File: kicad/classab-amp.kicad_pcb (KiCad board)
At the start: 2 copper layers, 62.6 x 114.6 mm, 75 parts, among them J3 INPUT, Q1 2N5401, Q10 IRFP9240, Q11 2N5551, Q12 2N5551, Q13 BD139, Q14 BD140, Q15 2N5551, Q16 BD140, Q2 2N5401, Q3 2N5401, Q4 2N5401, Q5 2N5551, Q6 2N5401, Q7 BD139, Q8 BD139, Q9 IRFP240

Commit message: Release candidate 1
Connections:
- net /LTP COM renamed Net-(Q2-E)

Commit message: Power supply work
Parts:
- R3, R5: value 470 -> 100
- R4: value 1k -> 470
- moved R5 9.59 mm to (231.4, 144.5)
- moved C11 3.22 mm to (239.8, 54.4)
- moved R3 1.78 mm to (231.4, 149.6)
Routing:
- net B+: track 146.5 -> 141.6 mm
- net Net-(Q5-E): track 11.6 -> 7.39 mm
- net Net-(C11-Pad2): track 12.1 -> 8.52 mm
- net Net-(Q11-E): track 11.4 -> 13.2 mm
- net PWRGND: track 351.6 -> 351.1 mm
- net B-: track 126.5 -> 126.0 mm

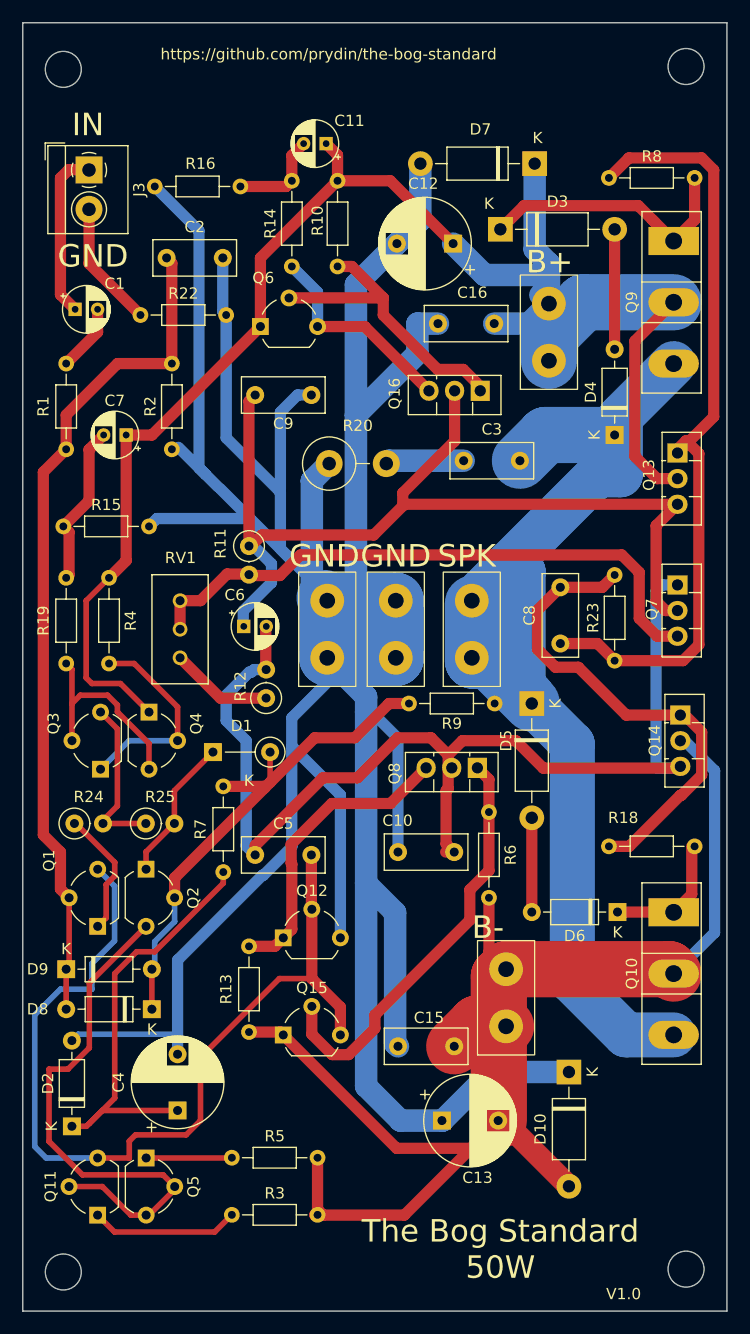
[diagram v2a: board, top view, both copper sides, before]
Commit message: Adjusted some component positioning
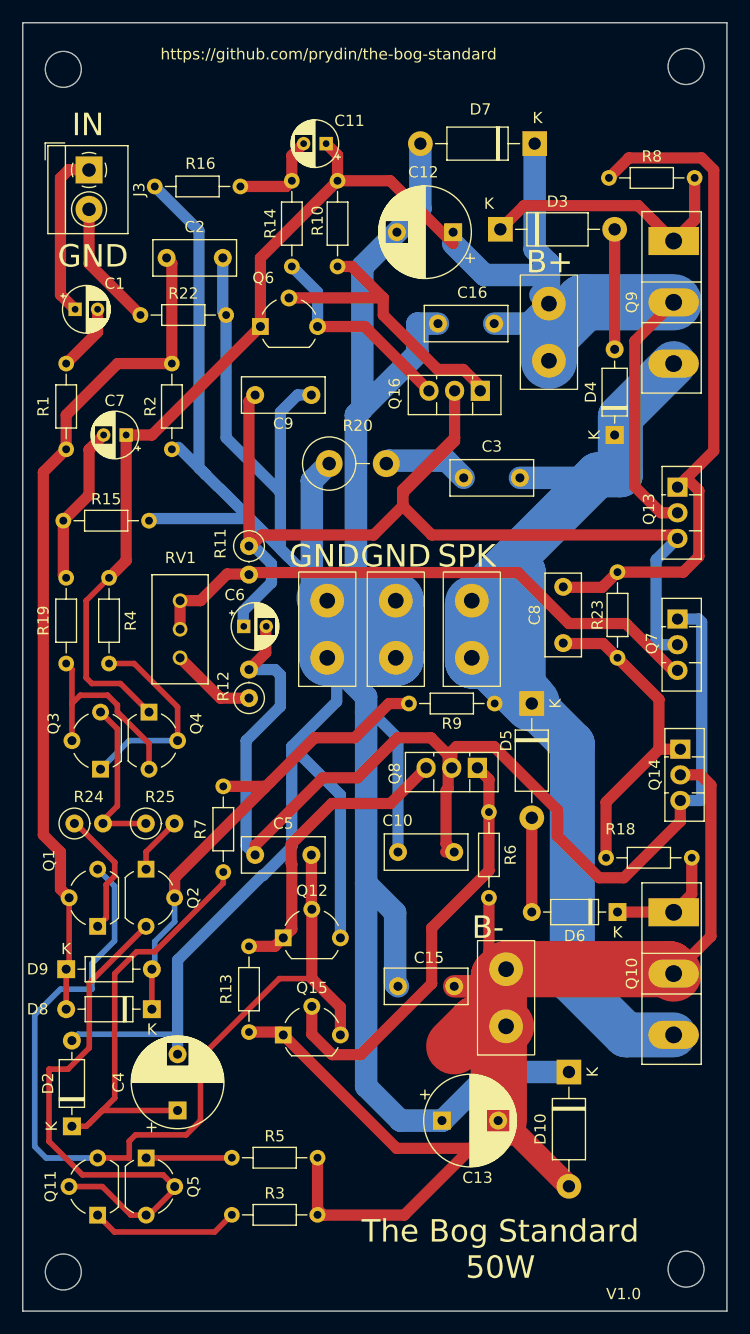
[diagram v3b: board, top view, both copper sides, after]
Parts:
- removed D1: 1N4148, Diode_THT:D_DO-35_SOD27_P5.08mm_Vertical_KathodeUp
- moved R23 7.88 mm to (265.7, 92.5), turned to -90 degrees
- moved C15 5.33 mm to (251.2, 129.3)
- moved C8 5.05 mm to (260.9, 93.8), turned to -90 degrees
- moved Q13 3.04 mm to (271.0, 84.9)
- moved Q7 3.04 mm to (271.0, 96.6)
- moved Q14 3.04 mm to (271.3, 108.2)
- moved D7 1.78 mm to (258.3, 54.4)
- moved C3 1.52 mm to (257.0, 84.1)
- moved R12 1.52 mm to (232.9, 103.7)
- moved R18 1.05 mm to (264.7, 117.9)
- moved C12 1.02 mm to (251.1, 62.2)
- moved R15 0.51 mm to (216.4, 87.9)
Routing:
- net Net-(Q14-E): track 43.6 -> 28.4 mm
- net Net-(Q14-B): track 97.6 -> 109.7 mm
- net Net-(Q13-E): track 70.2 -> 60.5 mm
- net Net-(Q13-B): track 86.2 -> 95.5 mm
- net Net-(Q2-E): track 12.9 -> 5.11 mm
- net B+: track 141.6 -> 146.2 mm
- net PWRGND: track 351.1 -> 347.3 mm
- net Net-(D8-K): track 45.8 -> 43.2 mm
- net Net-(Q7-B): track 54.0 -> 51.7 mm
- net /SPEAKER: track 105.8 -> 103.4 mm
- net B-: track 126.0 -> 128.2 mm
- net Net-(R12-Pad1): track 9.14 -> 7.61 mm
- net Net-(D6-K): track 11.5 -> 10.5 mm
- net Net-(C3-Pad2): track 6.99 -> 7.62 mm
- net Net-(Q15-B): track 37.6 -> 38.2 mm

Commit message: V1.1
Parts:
- removed the R22 at (223.3, 69.6)
- added J2: VOLUME, TerminalBlock_4Ucon:TerminalBlock_4Ucon_1x03_P3.50mm_Horizontal, F.Cu at (217.4, 70.5)
- added R2: 100, Resistor_THT:R_Axial_DIN0204_L3.6mm_D1.6mm_P7.62mm_Horizontal, F.Cu at (224.3, 68.3)
- added R3: 470, Resistor_THT:R_Axial_DIN0204_L3.6mm_D1.6mm_P7.62mm_Horizontal, F.Cu at (224.3, 72.1)
- C1: renamed from C2; value 100p -> 220p
- C6: renamed from C5; value 33p -> 47p
- C8: renamed from C9; value 68p -> 47p
- C9: renamed from C10; value 68p -> 47p
- R1: value 150 -> 1k
- R19: renamed from R10; value 47 -> 56
- R20: renamed from R6; value 22 -> 33
- moved C3 7.46 mm to (219.7, 76.2)
- moved R4 5.33 mm to (226.1, 76.2), turned to -90 degrees
- moved R1 3.06 mm to (216.4, 77.0)
- moved R16 2.29 mm to (232.2, 55.9)
- moved C2 1.78 mm to (222.0, 82.0)
- moved J1 1.76 mm to (217.4, 57.9), turned to 90 degrees
- moved C1 0.76 mm to (225.6, 63.8)
- moved R23 0.25 mm to (264.9, 117.9)
- renumbered C8 to C10, C16 to C11, C15 to C12, C12 to C13, C13 to C14, C3 to C15, C7 to C2, C1 to C3, C11 to C5, C6 to C7, D8 to D1, D9 to D2, D2 to D3, D3 to D4, D4 to D5, D5 to D6, D6 to D7, D7 to D8, D10 to D9, REF** to H1, REF** to H2, REF** to H3, REF** to H4, J3 to J1, J2 to J3, J1 to J5, J5 to J6, J6 to J7, Q4 to Q1, Q16 to Q10, Q7 to Q11, Q8 to Q12, Q9 to Q15, Q10 to Q16, Q1 to Q2, Q11 to Q3, Q3 to Q4, Q2 to Q6, Q15 to Q7, Q12 to Q8, Q6 to Q9, R25 to R10, R5 to R11, R7 to R12, R9 to R14, R14 to R15, R11 to R17, R12 to R18, R23 to R21, R8 to R22, R18 to R23, R20 to R24, R2 to R4, R19 to R5, R15 to R6, R3 to R7, R24 to R8, R4 to R9
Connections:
- C1 pad 1: Net-(D8-A) -> Net-(J2-Pin_3)
- C1 pad 2: PWRGND -> GNDS
- C3 pad 1: Net-(J3-Pin_1) -> Net-(D1-A)
- C3 pad 2: Net-(C1-Pad2) -> Net-(C3-Pad2)
- C4 pad 2: PWRGND -> GNDS
- D1 pad 2: Net-(D8-A) -> Net-(D1-A)
- D2 pad 1: Net-(D8-A) -> Net-(D1-A)
- D3 pad 2: PWRGND -> GNDS
- J1 pad 1: Net-(J3-Pin_1) -> GNDS
- J1 pad 2: GNDS -> Net-(J1-Pin_2)
- Q2 pad 2: Net-(D8-A) -> Net-(D1-A)
- R1 pad 1: Net-(C1-Pad2) -> Net-(J2-Pin_3)
- R1 pad 2: Net-(D8-A) -> Net-(J1-Pin_2)
- R4 pad 1: PWRGND -> GNDS
- R4 pad 2: Net-(D8-A) -> Net-(D1-A)
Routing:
- net GNDS: track 11.3 -> 136.9 mm
- net Net-(D8-A): track 75.0 -> 0.00 mm
- net Net-(D1-A): track 0.00 -> 63.8 mm
- net PWRGND: track 347.3 -> 299.5 mm
- net Net-(J1-Pin_2): track 0.00 -> 33.0 mm
- net Net-(J2-Pin_3): track 0.00 -> 22.6 mm
- net Net-(J3-Pin_1): track 15.0 -> 0.00 mm
- net Net-(C3-Pad2): track 0.00 -> 11.9 mm
- net B+: track 146.2 -> 157.4 mm
- net Net-(J2-Pin_2): track 0.00 -> 8.99 mm
- net Net-(C1-Pad2): track 5.98 -> 0.00 mm
- net B-: track 128.2 -> 123.4 mm
- net Net-(C2-Pad2): track 14.3 -> 12.5 mm
- net Net-(C5-Pad2): track 8.52 -> 9.47 mm
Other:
- board text added: "V1.1"
- board text removed: "V1.0"

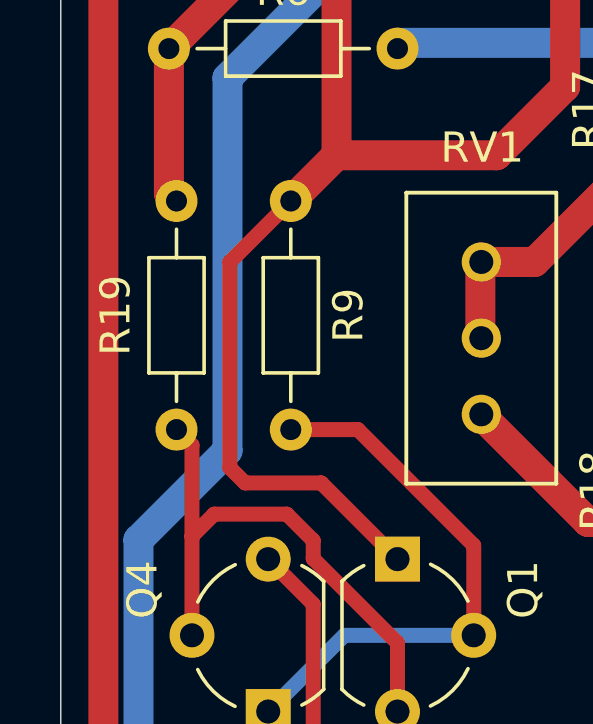
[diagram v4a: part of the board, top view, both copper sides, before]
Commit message: Fixed silkscreen typo
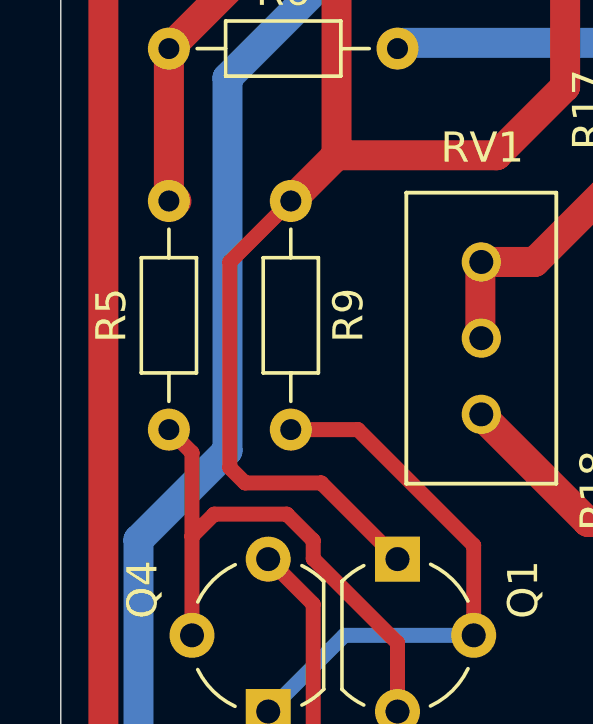
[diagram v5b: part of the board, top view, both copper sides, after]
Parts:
- R22, R23: value 47 -> 56
- moved R5 0.25 mm to (216.4, 100.6)
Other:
- board text removed: "R19"
